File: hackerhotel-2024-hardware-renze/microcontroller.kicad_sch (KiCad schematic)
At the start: 8 parts, among them U4 ESP32-C6-WROOM-1

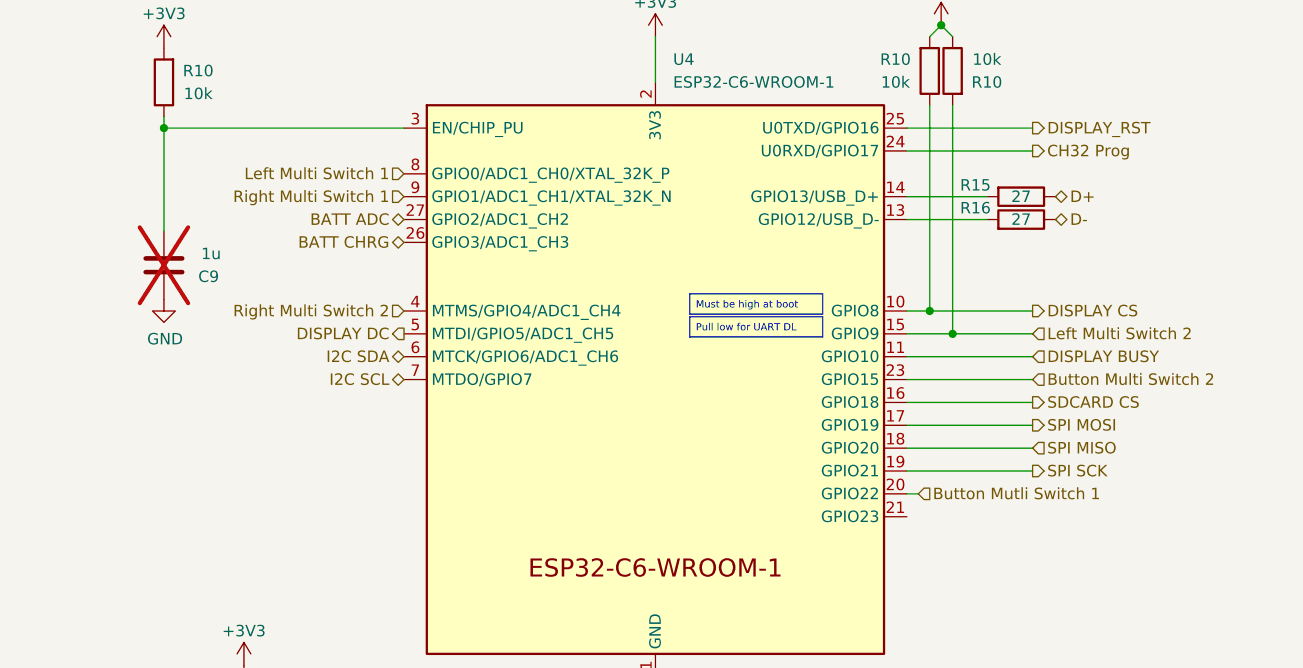
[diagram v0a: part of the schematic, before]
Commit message: V1.1 schematic
Added a relay for clicking noise
Multiplexed the switches and moved them all to the CH32
Wired an ESP32 low power triggered pin (GPIO4) to PC4 on the CH32 so it can wake it up on input change
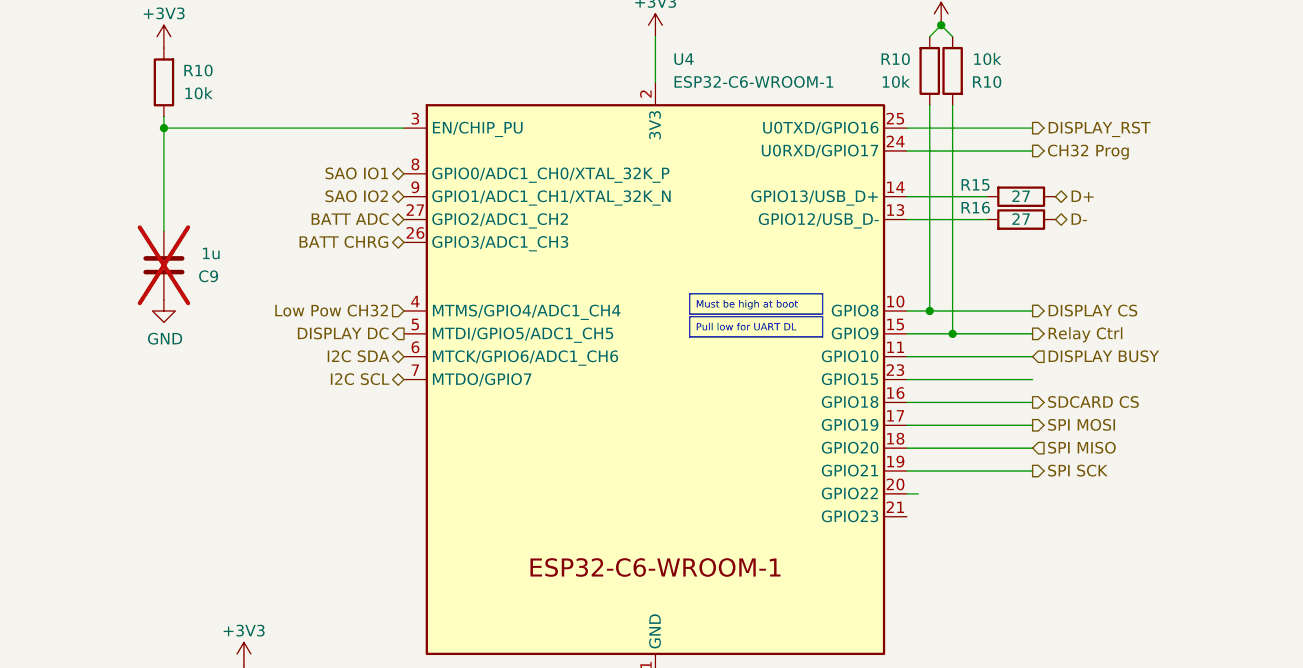
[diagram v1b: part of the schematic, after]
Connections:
- net Button Multi Switch 2: no longer names the net of U4.23 (GPIO15)
- net Button Mutli Switch 1: no longer names the net of U4.20 (GPIO22)
- net Left Multi Switch 1 renamed SAO IO1
- net Left Multi Switch 2 renamed Relay Ctrl
- net Right Multi Switch 1 renamed SAO IO2
- net Right Multi Switch 2 renamed Low Pow CH32
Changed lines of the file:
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@@
     (effects (font (size 1.27 1.27)) (justify left top))
+  )
+  (hierarchical_label "SAO IO2" (shape bidirectional) (at 116.84 71.12 180) (fields_autoplaced)
+    (effects (font (size 1.27 1.27)) (justify right))
   )
   (hierarchical_label "SPI MISO" (shape input) (at 186.69 99.06 0) (fields_autoplaced)
@@
     (effects (font (size 1.27 1.27)) (justify left))
   )
-  (hierarchical_label "Button Multi Switch 2" (shape input) (at 186.69 91.44 0) (fields_autoplaced)
-    (effects (font (size 1.27 1.27)) (justify left))
-  )
-  (hierarchical_label "Button Mutli Switch 1" (shape input) (at 173.99 104.14 0) (fields_autoplaced)
-    (effects (font (size 1.27 1.27)) (justify left))
-  )
   (hierarchical_label "SDCARD CS" (shape output) (at 186.69 93.98 0) (fields_autoplaced)
     (effects (font (size 1.27 1.27)) (justify left))
   )
-  (hierarchical_label "Left Multi Switch 1" (shape input) (at 116.84 68.58 180) (fields_autoplaced)
-    (effects (font (size 1.27 1.27)) (justify right))
-  )
   (hierarchical_label "DISPLAY_RST" (shape output) (at 186.69 63.5 0) (fields_autoplaced)
     (effects (font (size 1.27 1.27)) (justify left))
+  )
+  (hierarchical_label "SAO IO1" (shape bidirectional) (at 116.84 68.58 180) (fields_autoplaced)
+    (effects (font (size 1.27 1.27)) (justify right))
   )
   (hierarchical_label "I2C SCL" (shape bidirectional) (at 116.84 91.44 180) (fields_autoplaced)
@@
     (effects (font (size 1.27 1.27)) (justify right))
   )
-  (hierarchical_label "Right Multi Switch 2" (shape input) (at 116.84 83.82 180) (fields_autoplaced)
+  (hierarchical_label "Low Pow CH32" (shape input) (at 116.84 83.82 180) (fields_autoplaced)
     (effects (font (size 1.27 1.27)) (justify right))
   )
@@
     (effects (font (size 1.27 1.27)) (justify left))
   )
-  (hierarchical_label "Right Multi Switch 1" (shape input) (at 116.84 71.12 180) (fields_autoplaced)
-    (effects (font (size 1.27 1.27)) (justify right))
-  )
   (hierarchical_label "SPI SCK" (shape output) (at 186.69 101.6 0) (fields_autoplaced)
-    (effects (font (size 1.27 1.27)) (justify left))
-  )
-  (hierarchical_label "Left Multi Switch 2" (shape input) (at 186.69 86.36 0) (fields_autoplaced)
     (effects (font (size 1.27 1.27)) (justify left))
   )
@@
     (effects (font (size 1.27 1.27)) (justify left))
   )
+  (hierarchical_label "Relay Ctrl" (shape output) (at 186.69 86.36 0) (fields_autoplaced)
+    (effects (font (size 1.27 1.27)) (justify left))
+  )
